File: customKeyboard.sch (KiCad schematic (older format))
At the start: 160 parts, among them J1 USB_C_Receptacle_USB2.0, SW1 SW_Push, U1 ATmega32U4-AU, Y1 16MHz

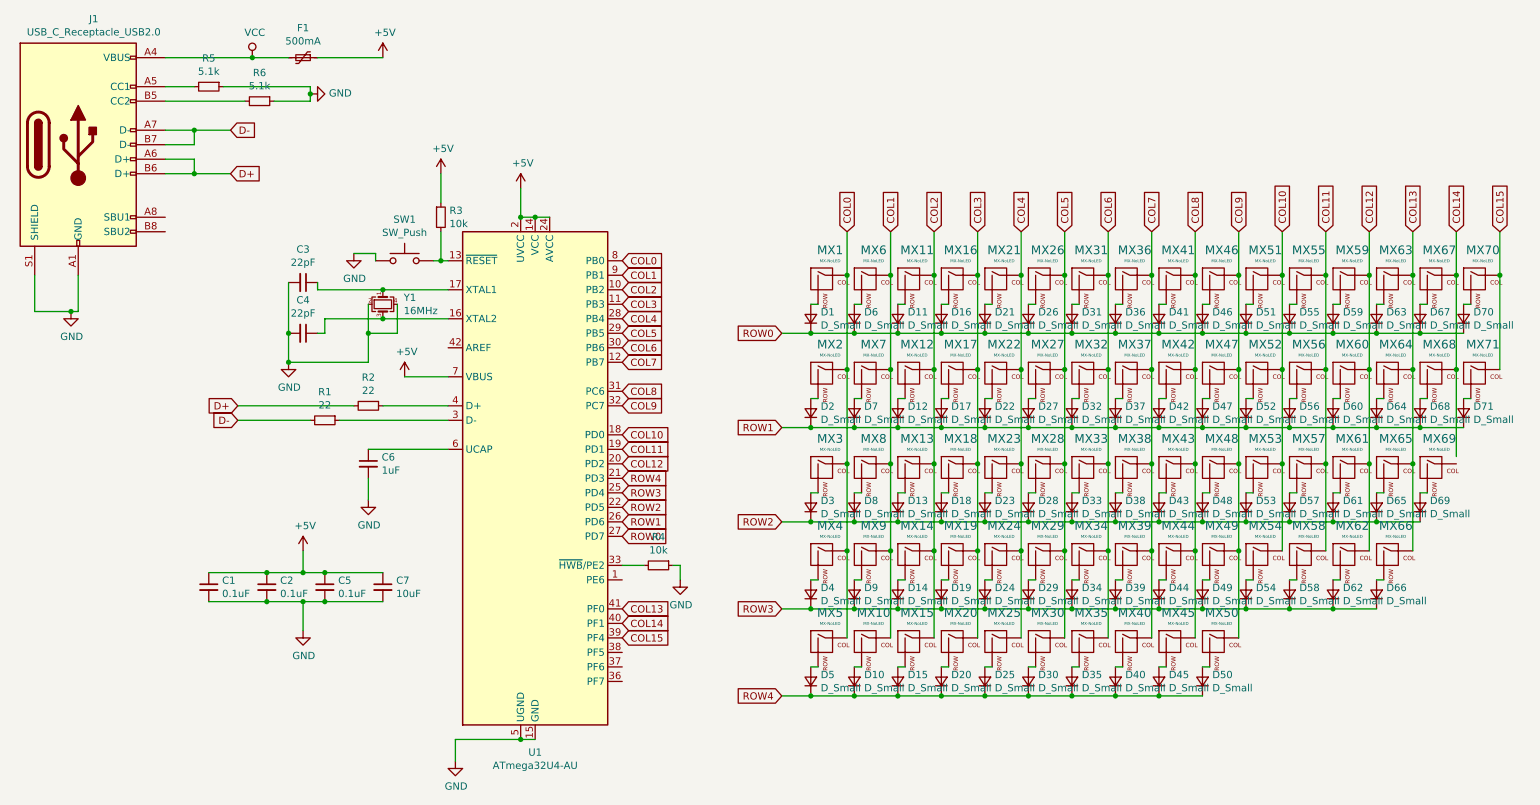
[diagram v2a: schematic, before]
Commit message: ROW and COL0 complete
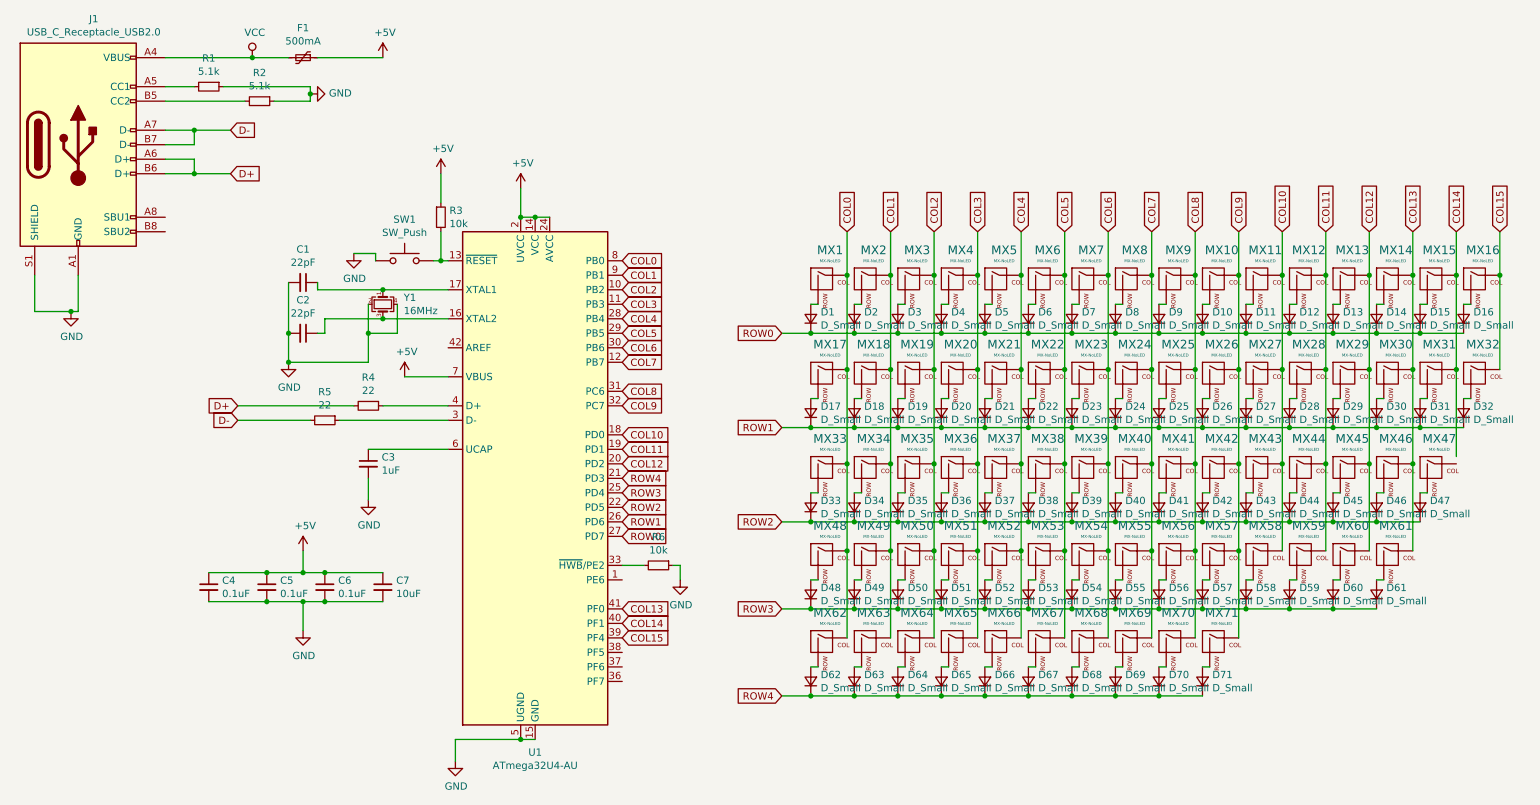
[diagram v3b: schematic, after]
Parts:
- renumbered C3 to C1, C4 to C2, C6 to C3, C1 to C4, C2 to C5, C5 to C6, D46 to D10, D51 to D11, D55 to D12, D59 to D13, D63 to D14, D67 to D15, D70 to D16, D2 to D17, D7 to D18, D12 to D19, D6 to D2, D17 to D20, D22 to D21, D27 to D22, D32 to D23, D37 to D24, D42 to D25, D47 to D26, D52 to D27, D56 to D28, D60 to D29, D11 to D3, D64 to D30, D68 to D31, D71 to D32, D3 to D33, D8 to D34, D13 to D35, D18 to D36, D23 to D37, D28 to D38, D33 to D39, D16 to D4, D38 to D40, D43 to D41, D48 to D42, D53 to D43, D57 to D44, D61 to D45, D65 to D46, D69 to D47, D4 to D48, D9 to D49, D21 to D5, D14 to D50, D19 to D51, D24 to D52, D29 to D53, D34 to D54, D39 to D55, D44 to D56, D49 to D57, D54 to D58, D58 to D59, D26 to D6, D62 to D60, D66 to D61, D5 to D62, D10 to D63, D15 to D64, D20 to D65, D25 to D66, D30 to D67, D35 to D68, D40 to D69, D31 to D7, D45 to D70, D50 to D71, D36 to D8, D41 to D9, MX46 to MX10, MX51 to MX11, MX55 to MX12, MX59 to MX13, MX63 to MX14, MX67 to MX15, MX70 to MX16, MX2 to MX17, MX7 to MX18, MX12 to MX19, MX6 to MX2, MX17 to MX20, MX22 to MX21, MX27 to MX22, MX32 to MX23, MX37 to MX24, MX42 to MX25, MX47 to MX26, MX52 to MX27, MX56 to MX28, MX60 to MX29, MX11 to MX3, MX64 to MX30, MX68 to MX31, MX71 to MX32, MX3 to MX33, MX8 to MX34, MX13 to MX35, MX18 to MX36, MX23 to MX37, MX28 to MX38, MX33 to MX39, MX16 to MX4, MX38 to MX40, MX43 to MX41, MX48 to MX42, MX53 to MX43, MX57 to MX44, MX61 to MX45, MX65 to MX46, MX69 to MX47, MX4 to MX48, MX9 to MX49, MX21 to MX5, MX14 to MX50, MX19 to MX51, MX24 to MX52, MX29 to MX53, MX34 to MX54, MX39 to MX55, MX44 to MX56, MX49 to MX57, MX54 to MX58, MX58 to MX59, MX26 to MX6, MX62 to MX60, MX66 to MX61, MX5 to MX62, MX10 to MX63, MX15 to MX64, MX20 to MX65, MX25 to MX66, MX30 to MX67, MX35 to MX68, MX40 to MX69, MX31 to MX7, MX45 to MX70, MX50 to MX71, MX36 to MX8, MX41 to MX9, R5 to R1, R6 to R2, R2 to R4, R1 to R5, R4 to R6

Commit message: 80% Complete
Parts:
- MX13: footprint MX_Alps_Hybrid:MX-2.75U -> MX_Alps_Hybrid:MX-1U
- MX14: footprint MX_Alps_Hybrid:MX-1.25U -> MX_Alps_Hybrid:MX-2U
- MX15, MX31, MX60, MX61: footprint MX_Alps_Hybrid:MX-1.25U -> MX_Alps_Hybrid:MX-1U
- MX17: footprint MX_Alps_Hybrid:MX-1U -> MX_Alps_Hybrid:MX-1.5U
- MX20: footprint MX_Alps_Hybrid:MX-1.5U -> MX_Alps_Hybrid:MX-1U
- MX30: footprint MX_Alps_Hybrid:MX-1.25U -> MX_Alps_Hybrid:MX-1.5U
- MX33: footprint MX_Alps_Hybrid:MX-1U -> MX_Alps_Hybrid:MX-1.75U
- MX39: footprint MX_Alps_Hybrid:MX-1.75U -> MX_Alps_Hybrid:MX-1U
- MX42, MX70: footprint MX_Alps_Hybrid:MX-2.25U -> MX_Alps_Hybrid:MX-1U
- MX45, MX48: footprint MX_Alps_Hybrid:MX-1U -> MX_Alps_Hybrid:MX-2.25U
- MX46: footprint MX_Alps_Hybrid:MX-6.25U -> MX_Alps_Hybrid:MX-1U
- MX50: footprint MX_Alps_Hybrid:MX-2U -> MX_Alps_Hybrid:MX-1U
- MX59: footprint MX_Alps_Hybrid:MX-1U -> MX_Alps_Hybrid:MX-2.75U
- MX62, MX63, MX64, MX66, MX68: footprint MX_Alps_Hybrid:MX-1U -> MX_Alps_Hybrid:MX-1.25U
- MX65: footprint MX_Alps_Hybrid:MX-1U -> MX_Alps_Hybrid:MX-6.25U
- MX67: footprint MX_Alps_Hybrid:MX-1.5U -> MX_Alps_Hybrid:MX-1.25U
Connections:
- net COL14: now also MX47.1 (COL)
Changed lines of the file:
@@
 F 0 "MX13" H 9883 2623 60  0000 C CNN
 F 1 "MX-NoLED" H 9883 2549 20  0000 C CNN
-F 2 "MX_Alps_Hybrid:MX-2.75U" H 9225 2375 60  0001 C CNN
+F 2 "MX_Alps_Hybrid:MX-1U" H 9225 2375 60  0001 C CNN
 F 3 "" H 9225 2375 60  0001 C CNN
 	1    9850 2400
@@
 F 0 "MX14" H 10183 2623 60  0000 C CNN
 F 1 "MX-NoLED" H 10183 2549 20  0000 C CNN
-F 2 "MX_Alps_Hybrid:MX-1.25U" H 9525 2375 60  0001 C CNN
+F 2 "MX_Alps_Hybrid:MX-2U" H 9525 2375 60  0001 C CNN
 F 3 "" H 9525 2375 60  0001 C CNN
 	1    10150 2400
@@
 F 0 "MX15" H 10483 2623 60  0000 C CNN
 F 1 "MX-NoLED" H 10483 2549 20  0000 C CNN
-F 2 "MX_Alps_Hybrid:MX-1.25U" H 9825 2375 60  0001 C CNN
+F 2 "MX_Alps_Hybrid:MX-1U" H 9825 2375 60  0001 C CNN
 F 3 "" H 9825 2375 60  0001 C CNN
 	1    10450 2400
@@
 F 0 "MX48" H 6283 4523 60  0000 C CNN
 F 1 "MX-NoLED" H 6283 4449 20  0000 C CNN
-F 2 "MX_Alps_Hybrid:MX-1U" H 5625 4275 60  0001 C CNN
+F 2 "MX_Alps_Hybrid:MX-2.25U" H 5625 4275 60  0001 C CNN
 F 3 "" H 5625 4275 60  0001 C CNN
 	1    6250 4300
@@
 F 0 "MX50" H 6883 4523 60  0000 C CNN
 F 1 "MX-NoLED" H 6883 4449 20  0000 C CNN
-F 2 "MX_Alps_Hybrid:MX-2U" H 6225 4275 60  0001 C CNN
+F 2 "MX_Alps_Hybrid:MX-1U" H 6225 4275 60  0001 C CNN
 F 3 "" H 6225 4275 60  0001 C CNN
 	1    6850 4300
@@
 F 0 "MX59" H 9583 4523 60  0000 C CNN
 F 1 "MX-NoLED" H 9583 4449 20  0000 C CNN
-F 2 "MX_Alps_Hybrid:MX-1U" H 8925 4275 60  0001 C CNN
+F 2 "MX_Alps_Hybrid:MX-2.75U" H 8925 4275 60  0001 C CNN
 F 3 "" H 8925 4275 60  0001 C CNN
 	1    9550 4300
@@
 F 0 "MX60" H 9883 4523 60  0000 C CNN
 F 1 "MX-NoLED" H 9883 4449 20  0000 C CNN
-F 2 "MX_Alps_Hybrid:MX-1.25U" H 9225 4275 60  0001 C CNN
+F 2 "MX_Alps_Hybrid:MX-1U" H 9225 4275 60  0001 C CNN
 F 3 "" H 9225 4275 60  0001 C CNN
 	1    9850 4300
@@
 F 0 "MX61" H 10183 4523 60  0000 C CNN
 F 1 "MX-NoLED" H 10183 4449 20  0000 C CNN
-F 2 "MX_Alps_Hybrid:MX-1.25U" H 9525 4275 60  0001 C CNN
+F 2 "MX_Alps_Hybrid:MX-1U" H 9525 4275 60  0001 C CNN
 F 3 "" H 9525 4275 60  0001 C CNN
 	1    10150 4300
@@
 F 0 "MX62" H 6283 5123 60  0000 C CNN
 F 1 "MX-NoLED" H 6283 5049 20  0000 C CNN
-F 2 "MX_Alps_Hybrid:MX-1U" H 5625 4875 60  0001 C CNN
+F 2 "MX_Alps_Hybrid:MX-1.25U" H 5625 4875 60  0001 C CNN
 F 3 "" H 5625 4875 60  0001 C CNN
 	1    6250 4900
@@
 F 0 "MX63" H 6583 5123 60  0000 C CNN
 F 1 "MX-NoLED" H 6583 5049 20  0000 C CNN
-F 2 "MX_Alps_Hybrid:MX-1U" H 5925 4875 60  0001 C CNN
+F 2 "MX_Alps_Hybrid:MX-1.25U" H 5925 4875 60  0001 C CNN
 F 3 "" H 5925 4875 60  0001 C CNN
 	1    6550 4900
@@
 F 0 "MX64" H 6883 5123 60  0000 C CNN
 F 1 "MX-NoLED" H 6883 5049 20  0000 C CNN
-F 2 "MX_Alps_Hybrid:MX-1U" H 6225 4875 60  0001 C CNN
+F 2 "MX_Alps_Hybrid:MX-1.25U" H 6225 4875 60  0001 C CNN
 F 3 "" H 6225 4875 60  0001 C CNN
 	1    6850 4900
@@
 F 0 "MX65" H 7183 5123 60  0000 C CNN
 F 1 "MX-NoLED" H 7183 5049 20  0000 C CNN
-F 2 "MX_Alps_Hybrid:MX-1U" H 6525 4875 60  0001 C CNN
+F 2 "MX_Alps_Hybrid:MX-6.25U" H 6525 4875 60  0001 C CNN
 F 3 "" H 6525 4875 60  0001 C CNN
 	1    7150 4900
@@
 F 0 "MX66" H 7483 5123 60  0000 C CNN
 F 1 "MX-NoLED" H 7483 5049 20  0000 C CNN
-F 2 "MX_Alps_Hybrid:MX-1U" H 6825 4875 60  0001 C CNN
+F 2 "MX_Alps_Hybrid:MX-1.25U" H 6825 4875 60  0001 C CNN
 F 3 "" H 6825 4875 60  0001 C CNN
 	1    7450 4900
@@
 F 0 "MX67" H 7783 5123 60  0000 C CNN
 F 1 "MX-NoLED" H 7783 5049 20  0000 C CNN
-F 2 "MX_Alps_Hybrid:MX-1.5U" H 7125 4875 60  0001 C CNN
+F 2 "MX_Alps_Hybrid:MX-1.25U" H 7125 4875 60  0001 C CNN
 F 3 "" H 7125 4875 60  0001 C CNN
 	1    7750 4900
@@
 F 0 "MX68" H 8083 5123 60  0000 C CNN
 F 1 "MX-NoLED" H 8083 5049 20  0000 C CNN
-F 2 "MX_Alps_Hybrid:MX-1U" H 7425 4875 60  0001 C CNN
+F 2 "MX_Alps_Hybrid:MX-1.25U" H 7425 4875 60  0001 C CNN
 F 3 "" H 7425 4875 60  0001 C CNN
 	1    8050 4900
@@
 F 0 "MX70" H 8683 5123 60  0000 C CNN
 F 1 "MX-NoLED" H 8683 5049 20  0000 C CNN
-F 2 "MX_Alps_Hybrid:MX-2.25U" H 8025 4875 60  0001 C CNN
+F 2 "MX_Alps_Hybrid:MX-1U" H 8025 4875 60  0001 C CNN
 F 3 "" H 8025 4875 60  0001 C CNN
 	1    8650 4900
@@
 F 0 "MX17" H 6283 3273 60  0000 C CNN
 F 1 "MX-NoLED" H 6283 3199 20  0000 C CNN
-F 2 "MX_Alps_Hybrid:MX-1U" H 5625 3025 60  0001 C CNN
+F 2 "MX_Alps_Hybrid:MX-1.5U" H 5625 3025 60  0001 C CNN
 F 3 "" H 5625 3025 60  0001 C CNN
 	1    6250 3050
@@
 F 0 "MX20" H 7183 3273 60  0000 C CNN
 F 1 "MX-NoLED" H 7183 3199 20  0000 C CNN
-F 2 "MX_Alps_Hybrid:MX-1.5U" H 6525 3025 60  0001 C CNN
+F 2 "MX_Alps_Hybrid:MX-1U" H 6525 3025 60  0001 C CNN
 F 3 "" H 6525 3025 60  0001 C CNN
 	1    7150 3050
@@
 F 0 "MX30" H 10183 3273 60  0000 C CNN
 F 1 "MX-NoLED" H 10183 3199 20  0000 C CNN
-F 2 "MX_Alps_Hybrid:MX-1.25U" H 9525 3025 60  0001 C CNN
+F 2 "MX_Alps_Hybrid:MX-1.5U" H 9525 3025 60  0001 C CNN
 F 3 "" H 9525 3025 60  0001 C CNN
 	1    10150 3050
@@
 F 0 "MX31" H 10483 3273 60  0000 C CNN
 F 1 "MX-NoLED" H 10483 3199 20  0000 C CNN
-F 2 "MX_Alps_Hybrid:MX-1.25U" H 9825 3025 60  0001 C CNN
+F 2 "MX_Alps_Hybrid:MX-1U" H 9825 3025 60  0001 C CNN
 F 3 "" H 9825 3025 60  0001 C CNN
 	1    10450 3050
@@
 F 0 "MX33" H 6283 3923 60  0000 C CNN
 F 1 "MX-NoLED" H 6283 3849 20  0000 C CNN
-F 2 "MX_Alps_Hybrid:MX-1U" H 5625 3675 60  0001 C CNN
+F 2 "MX_Alps_Hybrid:MX-1.75U" H 5625 3675 60  0001 C CNN
 F 3 "" H 5625 3675 60  0001 C CNN
 	1    6250 3700
@@
 F 0 "MX39" H 8083 3923 60  0000 C CNN
 F 1 "MX-NoLED" H 8083 3849 20  0000 C CNN
-F 2 "MX_Alps_Hybrid:MX-1.75U" H 7425 3675 60  0001 C CNN
+F 2 "MX_Alps_Hybrid:MX-1U" H 7425 3675 60  0001 C CNN
 F 3 "" H 7425 3675 60  0001 C CNN
 	1    8050 3700
@@
 F 0 "MX42" H 8983 3923 60  0000 C CNN
 F 1 "MX-NoLED" H 8983 3849 20  0000 C CNN
-F 2 "MX_Alps_Hybrid:MX-2.25U" H 8325 3675 60  0001 C CNN
+F 2 "MX_Alps_Hybrid:MX-1U" H 8325 3675 60  0001 C CNN
 F 3 "" H 8325 3675 60  0001 C CNN
 	1    8950 3700
@@
 F 0 "MX45" H 9883 3923 60  0000 C CNN
 F 1 "MX-NoLED" H 9883 3849 20  0000 C CNN
-F 2 "MX_Alps_Hybrid:MX-1U" H 9225 3675 60  0001 C CNN
+F 2 "MX_Alps_Hybrid:MX-2.25U" H 9225 3675 60  0001 C CNN
 F 3 "" H 9225 3675 60  0001 C CNN
 	1    9850 3700
@@
 F 0 "MX46" H 10183 3923 60  0000 C CNN
 F 1 "MX-NoLED" H 10183 3849 20  0000 C CNN
-F 2 "MX_Alps_Hybrid:MX-6.25U" H 9525 3675 60  0001 C CNN
+F 2 "MX_Alps_Hybrid:MX-1U" H 9525 3675 60  0001 C CNN
 F 3 "" H 9525 3675 60  0001 C CNN
 	1    10150 3700
@@
 Wire Wire Line
 	10600 2050 10600 2350
-Wire Wire Line
-	10600 3600 10600 3000
 Wire Wire Line
 	10600 3000 10600 2350
@@
 Text GLabel 4850 4850 2    50   Input ~ 0
 COL15
+Wire Wire Line
+	10600 3000 10600 3650
 $EndSCHEMATC
